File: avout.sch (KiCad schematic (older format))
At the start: 24 parts, among them CN6 AUDIO_VIDEO, M1 Modulator, Q3 2SC1815

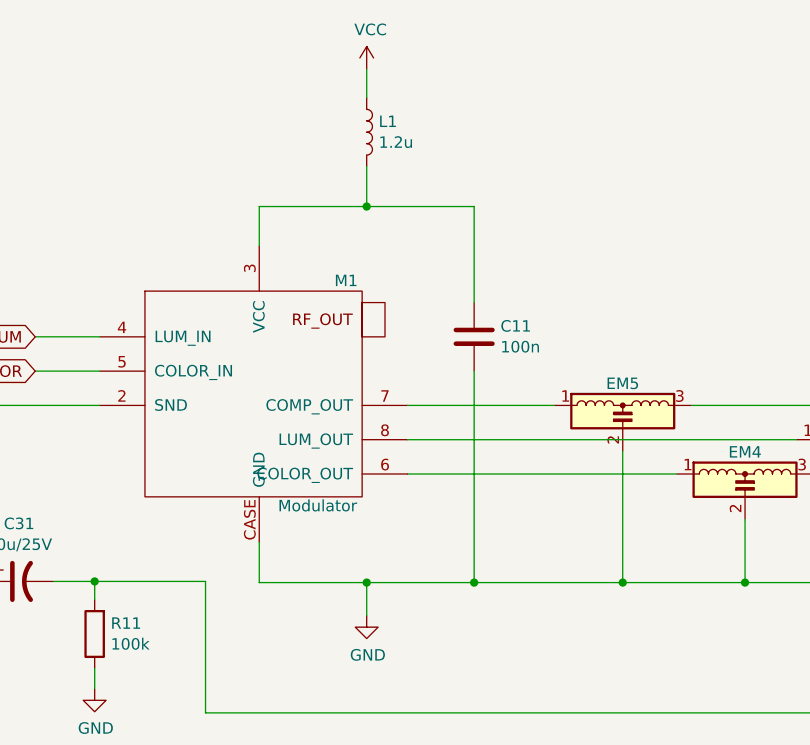
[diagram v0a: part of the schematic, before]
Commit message: Fix some errors pointed out by bwack in #1
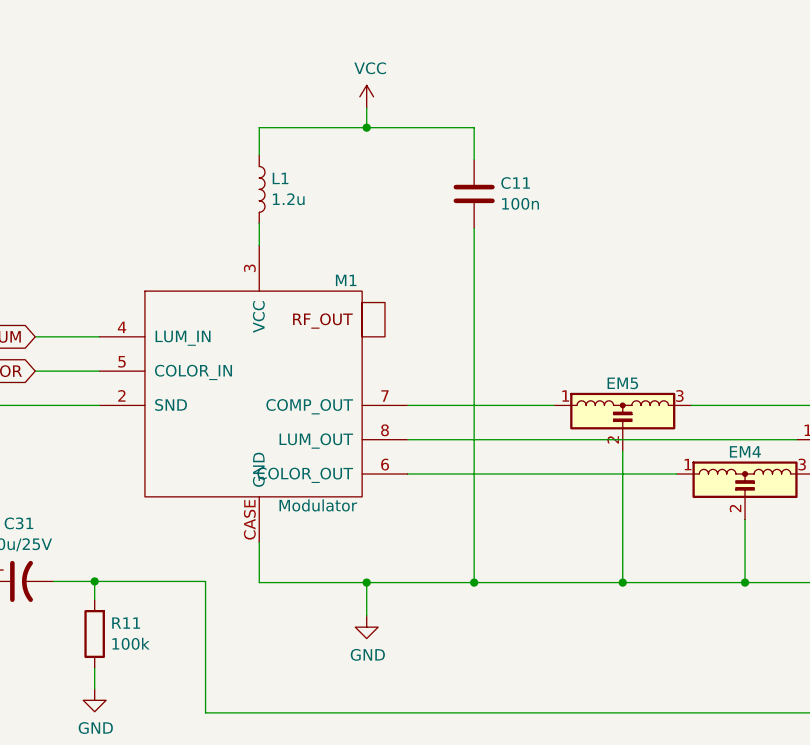
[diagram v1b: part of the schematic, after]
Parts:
- C11, C20: footprint (none) -> Capacitor_THT:C_Disc_D8.0mm_W2.5mm_P5.00mm
- C18, C19: footprint (none) -> Capacitor_THT:CP_Radial_D5.0mm_P2.50mm
- C31: footprint (none) -> Capacitor_THT:CP_Radial_D6.3mm_P2.50mm
- CN6: footprint (none) -> CommodorePlus4:Connector_DIN_Female_8Pin_3rows
- EM3, EM4, EM5: footprint (none) -> LittleSixteen:EMI_Filter
- FB12, FB13, FB58: footprint (none) -> LittleSixteen:Ferrite
- M1: footprint (none) -> CommodorePlus4:RF_Modulator
- Q3: footprint Package_TO_SOT_THT:TO-92_Inline -> Package_TO_SOT_THT:TO-92_Inline_Wide
- R11, R23, R24, R25, R26, R27, R28, R8, R9: footprint (none) -> Resistor_THT:R_Axial_DIN0207_L6.3mm_D2.5mm_P5.08mm_Vertical
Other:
- moved on the sheet: C11, L1
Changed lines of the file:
@@
 Sheet 11 11
 Title "LittleSixteen"
-Date "2020-01-03"
+Date "2020-10-04"
 Rev "1git"
 Comp "SukkoPera"
@@
 F 0 "M1" H 6440 3425 50  0000 C CNN
 F 1 "Modulator" H 6315 2440 50  0000 C CNN
-F 2 "" H 6260 2980 50  0001 C CNN
+F 2 "CommodorePlus4:RF_Modulator" H 6260 2980 50  0001 C CNN
 F 3 "" H 6260 2980 50  0001 C CNN
 	1    6060 2930
@@
 L Device:C C11
 U 1 1 5E01CA58
-P 7000 2680
-F 0 "C11" H 7115 2726 50  0000 L CNN
-F 1 "100n" H 7115 2635 50  0000 L CNN
-F 2 "" H 7038 2530 50  0001 C CNN
-F 3 "~" H 7000 2680 50  0001 C CNN
-	1    7000 2680
-	1    0    0    -1
-$EndComp
-Wire Wire Line
-	6060 2110 6530 2110
-Wire Wire Line
-	7000 2110 7000 2530
-Wire Wire Line
-	7000 2830 7000 3755
+P 7000 2055
+F 0 "C11" H 7115 2101 50  0000 L CNN
+F 1 "100n" H 7115 2010 50  0000 L CNN
+F 2 "Capacitor_THT:C_Disc_D8.0mm_W2.5mm_P5.00mm" H 7038 1905 50  0001 C CNN
+F 3 "~" H 7000 2055 50  0001 C CNN
+	1    7000 2055
+	1    0    0    -1
+$EndComp
+Wire Wire Line
+	7000 2205 7000 3755
 Wire Wire Line
 	7000 3755 6530 3755
@@
 L Device:L L1
 U 1 1 5E01E939
-P 6530 1785
-F 0 "L1" H 6582 1831 50  0000 L CNN
-F 1 "1.2u" H 6582 1740 50  0000 L CNN
-F 2 "" H 6530 1785 50  0001 C CNN
-F 3 "~" H 6530 1785 50  0001 C CNN
-	1    6530 1785
-	1    0    0    -1
-$EndComp
-Wire Wire Line
-	6530 1935 6530 2110
-Connection ~ 6530 2110
-Wire Wire Line
-	6530 2110 7000 2110
+P 6060 2035
+F 0 "L1" H 6112 2081 50  0000 L CNN
+F 1 "1.2u" H 6112 1990 50  0000 L CNN
+F 2 "" H 6060 2035 50  0001 C CNN
+F 3 "~" H 6060 2035 50  0001 C CNN
+	1    6060 2035
+	1    0    0    -1
+$EndComp
 $Comp
 L power:VCC #PWR0178
 U 1 1 5E021287
-P 6530 1510
-F 0 "#PWR0178" H 6530 1360 50  0001 C CNN
-F 1 "VCC" H 6547 1683 50  0000 C CNN
-F 2 "" H 6530 1510 50  0001 C CNN
-F 3 "" H 6530 1510 50  0001 C CNN
-	1    6530 1510
-	1    0    0    -1
-$EndComp
-Wire Wire Line
-	6530 1510 6530 1635
+P 6530 1680
+F 0 "#PWR0178" H 6530 1530 50  0001 C CNN
+F 1 "VCC" H 6547 1853 50  0000 C CNN
+F 2 "" H 6530 1680 50  0001 C CNN
+F 3 "" H 6530 1680 50  0001 C CNN
+	1    6530 1680
+	1    0    0    -1
+$EndComp
+Wire Wire Line
+	6530 1680 6530 1765
 $Comp
 L Connector:DIN-8 CN6
@@
 F 0 "CN6" H 9695 3725 50  0000 C CNN
 F 1 "AUDIO_VIDEO" H 9695 3640 50  0000 C CNN
-F 2 "" H 9695 3130 50  0001 C CNN
+F 2 "CommodorePlus4:Connector_DIN_Female_8Pin_3rows" H 9695 3130 50  0001 C CNN
 F 3 "http://www.mouser.com/ds/2/18/40_c091_abd_e-75918.pdf" H 9695 3130 50  0001 C CNN
 	1    9695 3130
@@
 F 0 "EM5" H 7650 3275 50  0000 C CNN
 F 1 "EMI_Filter_LCL" H 7650 3306 50  0001 C CNN
-F 2 "" V 7650 3080 50  0001 C CNN
+F 2 "LittleSixteen:EMI_Filter" V 7650 3080 50  0001 C CNN
 F 3 "http://www.murata.com/~/media/webrenewal/support/library/catalog/products/emc/emifil/c31e.ashx?la=en-gb" V 7650 3080 50  0001 C CNN
 	1    7650 3080
@@
 F 0 "EM3" H 8710 3425 50  0000 C CNN
 F 1 "EMI_Filter_LCL" H 8710 3456 50  0001 C CNN
-F 2 "" V 8710 3230 50  0001 C CNN
+F 2 "LittleSixteen:EMI_Filter" V 8710 3230 50  0001 C CNN
 F 3 "http://www.murata.com/~/media/webrenewal/support/library/catalog/products/emc/emifil/c31e.ashx?la=en-gb" V 8710 3230 50  0001 C CNN
 	1    8710 3230
@@
 F 0 "EM4" H 8185 3575 50  0000 C CNN
 F 1 "EMI_Filter_LCL" H 8185 3606 50  0001 C CNN
-F 2 "" V 8185 3380 50  0001 C CNN
+F 2 "LittleSixteen:EMI_Filter" V 8185 3380 50  0001 C CNN
 F 3 "http://www.murata.com/~/media/webrenewal/support/library/catalog/products/emc/emifil/c31e.ashx?la=en-gb" V 8185 3380 50  0001 C CNN
 	1    8185 3380
@@
 F 0 "FB13" H 10200 3530 50  0000 L CNN
 F 1 "Ferrite_Bead_Small" H 10200 3485 50  0001 L CNN
-F 2 "" V 10030 3530 50  0001 C CNN
+F 2 "LittleSixteen:Ferrite" V 10030 3530 50  0001 C CNN
 F 3 "~" H 10100 3530 50  0001 C CNN
 	1    10100 3530
@@
 F 0 "FB12" V 10360 3130 50  0000 C CNN
 F 1 "Ferrite_Bead_Small" H 10605 3085 50  0001 L CNN
-F 2 "" V 10435 3130 50  0001 C CNN
+F 2 "LittleSixteen:Ferrite" V 10435 3130 50  0001 C CNN
 F 3 "~" H 10505 3130 50  0001 C CNN
 	1    10505 3130
@@
 F 0 "FB58" V 10160 3030 50  0000 C CNN
 F 1 "Ferrite_Bead_Small" H 10405 2985 50  0001 L CNN
-F 2 "" V 10235 3030 50  0001 C CNN
+F 2 "LittleSixteen:Ferrite" V 10235 3030 50  0001 C CNN
 F 3 "~" H 10305 3030 50  0001 C CNN
 	1    10305 3030
@@
 F 0 "R28" V 1568 2780 50  0000 C CNN
 F 1 "1k" V 1659 2780 50  0000 C CNN
-F 2 "" V 1705 2780 50  0001 C CNN
+F 2 "Resistor_THT:R_Axial_DIN0207_L6.3mm_D2.5mm_P5.08mm_Vertical" V 1705 2780 50  0001 C CNN
 F 3 "~" H 1775 2780 50  0001 C CNN
 	1    1775 2780
@@
 F 0 "R25" H 1570 3046 50  0000 L CNN
 F 1 "100k" H 1570 2955 50  0000 L CNN
-F 2 "" V 1430 3000 50  0001 C CNN
+F 2 "Resistor_THT:R_Axial_DIN0207_L6.3mm_D2.5mm_P5.08mm_Vertical" V 1430 3000 50  0001 C CNN
 F 3 "~" H 1500 3000 50  0001 C CNN
 	1    1500 3000
@@
 F 0 "C18" V 1943 2780 50  0000 C CNN
 F 1 "10u/25V" V 2034 2780 50  0000 C CNN
-F 2 "" H 2195 2780 50  0001 C CNN
+F 2 "Capacitor_THT:CP_Radial_D5.0mm_P2.50mm" H 2195 2780 50  0001 C CNN
 F 3 "~" H 2195 2780 50  0001 C CNN
 	1    2195 2780
@@
 F 0 "R8" V 1568 2265 50  0000 C CNN
 F 1 "1k" V 1659 2265 50  0000 C CNN
-F 2 "" V 1705 2265 50  0001 C CNN
+F 2 "Resistor_THT:R_Axial_DIN0207_L6.3mm_D2.5mm_P5.08mm_Vertical" V 1705 2265 50  0001 C CNN
 F 3 "~" H 1775 2265 50  0001 C CNN
 	1    1775 2265
@@
 F 0 "C19" V 1943 2265 50  0000 C CNN
 F 1 "10u/25V" V 2034 2265 50  0000 C CNN
-F 2 "" H 2195 2265 50  0001 C CNN
+F 2 "Capacitor_THT:CP_Radial_D5.0mm_P2.50mm" H 2195 2265 50  0001 C CNN
 F 3 "~" H 2195 2265 50  0001 C CNN
 	1    2195 2265
@@
 F 0 "R24" V 3298 2515 50  0000 C CNN
 F 1 "1k" V 3389 2515 50  0000 C CNN
-F 2 "" V 3435 2515 50  0001 C CNN
+F 2 "Resistor_THT:R_Axial_DIN0207_L6.3mm_D2.5mm_P5.08mm_Vertical" V 3435 2515 50  0001 C CNN
 F 3 "~" H 3505 2515 50  0001 C CNN
 	1    3505 2515
@@
 F 0 "R9" H 2905 2826 50  0000 L CNN
 F 1 "12k" H 2905 2735 50  0000 L CNN
-F 2 "" V 2765 2780 50  0001 C CNN
+F 2 "Resistor_THT:R_Axial_DIN0207_L6.3mm_D2.5mm_P5.08mm_Vertical" V 2765 2780 50  0001 C CNN
 F 3 "~" H 2835 2780 50  0001 C CNN
 	1    2835 2780
@@
 F 0 "C20" H 3255 2826 50  0000 L CNN
 F 1 "10n" H 3255 2735 50  0000 L CNN
-F 2 "" H 3178 2630 50  0001 C CNN
+F 2 "Capacitor_THT:C_Disc_D8.0mm_W2.5mm_P5.00mm" H 3178 2630 50  0001 C CNN
 F 3 "~" H 3140 2780 50  0001 C CNN
 	1    3140 2780
@@
 F 0 "Q3" H 4180 2561 50  0000 L CNN
 F 1 "2SC1815" H 4180 2470 50  0000 L CNN
-F 2 "Package_TO_SOT_THT:TO-92_Inline" H 4190 2440 50  0001 L CIN
+F 2 "Package_TO_SOT_THT:TO-92_Inline_Wide" H 4190 2440 50  0001 L CIN
 F 3 "https://media.digikey.com/pdf/Data%20Sheets/Toshiba%20PDFs/2SC1815.pdf" H 3990 2515 50  0001 L CNN
 	1    3990 2515
@@
 F 0 "R23" H 3210 2246 50  0000 L CNN
 F 1 "10k" H 3210 2155 50  0000 L CNN
-F 2 "" V 3070 2200 50  0001 C CNN
+F 2 "Resistor_THT:R_Axial_DIN0207_L6.3mm_D2.5mm_P5.08mm_Vertical" V 3070 2200 50  0001 C CNN
 F 3 "~" H 3140 2200 50  0001 C CNN
 	1    3140 2200
@@
 F 0 "R26" V 4133 3750 50  0000 C CNN
 F 1 "240" V 4224 3750 50  0000 C CNN
-F 2 "" V 4270 3750 50  0001 C CNN
+F 2 "Resistor_THT:R_Axial_DIN0207_L6.3mm_D2.5mm_P5.08mm_Vertical" V 4270 3750 50  0001 C CNN
 F 3 "~" H 4340 3750 50  0001 C CNN
 	1    4340 3750
@@
 F 0 "R27" H 4600 3934 50  0000 R CNN
 F 1 "240" H 4600 4025 50  0000 R CNN
-F 2 "" V 4600 3980 50  0001 C CNN
+F 2 "Resistor_THT:R_Axial_DIN0207_L6.3mm_D2.5mm_P5.08mm_Vertical" V 4600 3980 50  0001 C CNN
 F 3 "~" H 4670 3980 50  0001 C CNN
 	1    4670 3980
@@
 F 0 "C31" V 4758 3750 50  0000 C CNN
 F 1 "10u/25V" V 4849 3750 50  0000 C CNN
-F 2 "" H 5010 3750 50  0001 C CNN
+F 2 "Capacitor_THT:CP_Radial_D6.3mm_P2.50mm" H 5010 3750 50  0001 C CNN
 F 3 "~" H 5010 3750 50  0001 C CNN
 	1    5010 3750
@@
 F 0 "R11" H 5270 3934 50  0000 R CNN
 F 1 "100k" H 5270 4025 50  0000 R CNN
-F 2 "" V 5270 3980 50  0001 C CNN
+F 2 "Resistor_THT:R_Axial_DIN0207_L6.3mm_D2.5mm_P5.08mm_Vertical" V 5270 3980 50  0001 C CNN
 F 3 "~" H 5340 3980 50  0001 C CNN
 	1    5340 3980
@@
 	4090 1780 4090 1875
 Connection ~ 4090 1875
-Wire Wire Line
-	6060 2280 6060 2110
 Text Notes 10670 3010 0    50   ~ 0
 EXT_AUDIO
@@
 Text Notes 8575 2360 0    50   ~ 0
 From C64-Wiki (C64 uses the same connector):\n\nThe eight pin jack is *not* the more common DIN 45326\n(pins spanning 270°, circular like a horseshoe), but\nDIN 41524 (pins spanning 262°, a "U" shape with a more\nopen end). It's possible to forcibly plug in a wrong plug into\nthe jack, but one should get the right plug in the first place\non a new purchase. Should you happen to get the wrong\nplug and wasn't planning to use the +5V pin then you can\nremove the upper two pins out for a perfect fit.
+Wire Wire Line
+	6530 1765 7000 1765
+Connection ~ 6530 1765
+Wire Wire Line
+	7000 1765 7000 1905
+Wire Wire Line
+	6530 1765 6060 1765
+Wire Wire Line
+	6060 1765 6060 1885
+Wire Wire Line
+	6060 2185 6060 2280
 $EndSCHEMATC

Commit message: Start working on PCB
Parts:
- C18, C19: footprint Capacitor_THT:CP_Radial_D5.0mm_P2.50mm -> Capacitor_THT:CP_Radial_D6.3mm_P2.50mm
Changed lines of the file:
@@
 F 0 "C18" V 1943 2780 50  0000 C CNN
 F 1 "10u/25V" V 2034 2780 50  0000 C CNN
-F 2 "Capacitor_THT:CP_Radial_D5.0mm_P2.50mm" H 2195 2780 50  0001 C CNN
+F 2 "Capacitor_THT:CP_Radial_D6.3mm_P2.50mm" H 2195 2780 50  0001 C CNN
 F 3 "~" H 2195 2780 50  0001 C CNN
 	1    2195 2780
@@
 F 0 "C19" V 1943 2265 50  0000 C CNN
 F 1 "10u/25V" V 2034 2265 50  0000 C CNN
-F 2 "Capacitor_THT:CP_Radial_D5.0mm_P2.50mm" H 2195 2265 50  0001 C CNN
+F 2 "Capacitor_THT:CP_Radial_D6.3mm_P2.50mm" H 2195 2265 50  0001 C CNN
 F 3 "~" H 2195 2265 50  0001 C CNN
 	1    2195 2265

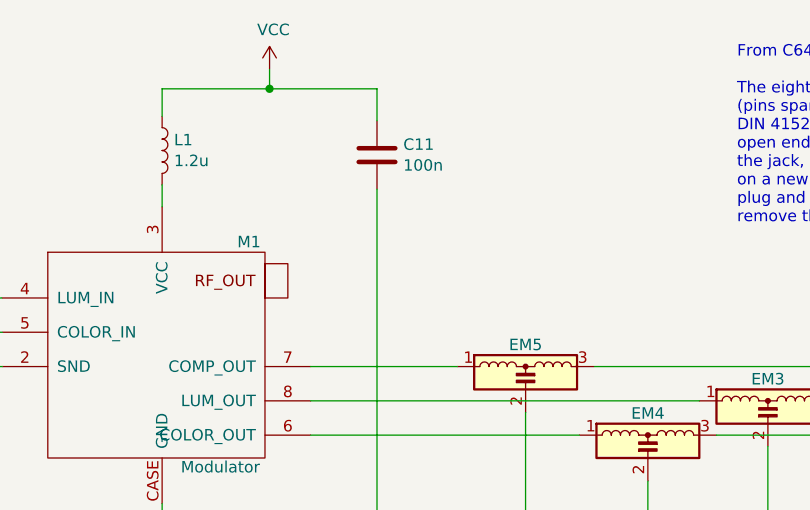
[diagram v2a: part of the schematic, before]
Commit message: Add ceramics
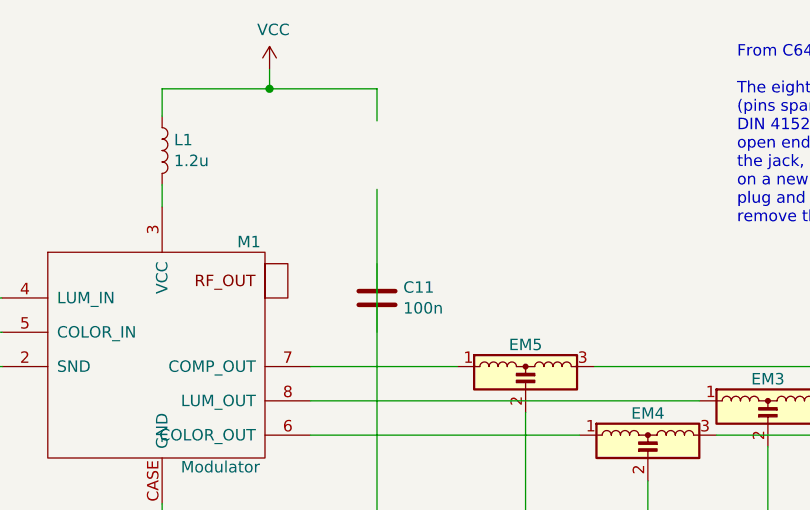
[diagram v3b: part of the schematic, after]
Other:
- moved on the sheet: C11
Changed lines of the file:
@@
 L Device:C C11
 U 1 1 5E01CA58
-P 7000 2055
-F 0 "C11" H 7115 2101 50  0000 L CNN
-F 1 "100n" H 7115 2010 50  0000 L CNN
-F 2 "Capacitor_THT:C_Disc_D8.0mm_W2.5mm_P5.00mm" H 7038 1905 50  0001 C CNN
-F 3 "~" H 7000 2055 50  0001 C CNN
-	1    7000 2055
+P 7000 2680
+F 0 "C11" H 7115 2726 50  0000 L CNN
+F 1 "100n" H 7115 2635 50  0000 L CNN
+F 2 "Capacitor_THT:C_Disc_D8.0mm_W2.5mm_P5.00mm" H 7038 2530 50  0001 C CNN
+F 3 "~" H 7000 2680 50  0001 C CNN
+	1    7000 2680
 	1    0    0    -1
 $EndComp

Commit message: Add crystal
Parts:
- C18, C19: footprint Capacitor_THT:CP_Radial_D6.3mm_P2.50mm -> Capacitor_THT:CP_Radial_D5.0mm_P2.50mm
- EM3, EM4, EM5: footprint LittleSixteen:EMI_Filter -> CSeventeen:EMI_Filter
- FB12, FB13, FB58: footprint LittleSixteen:Ferrite -> CSeventeen:Ferrite
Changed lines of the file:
@@
 F 0 "EM5" H 7650 3275 50  0000 C CNN
 F 1 "EMI_Filter_LCL" H 7650 3306 50  0001 C CNN
-F 2 "LittleSixteen:EMI_Filter" V 7650 3080 50  0001 C CNN
+F 2 "CSeventeen:EMI_Filter" V 7650 3080 50  0001 C CNN
 F 3 "http://www.murata.com/~/media/webrenewal/support/library/catalog/products/emc/emifil/c31e.ashx?la=en-gb" V 7650 3080 50  0001 C CNN
 	1    7650 3080
@@
 F 0 "EM3" H 8710 3425 50  0000 C CNN
 F 1 "EMI_Filter_LCL" H 8710 3456 50  0001 C CNN
-F 2 "LittleSixteen:EMI_Filter" V 8710 3230 50  0001 C CNN
+F 2 "CSeventeen:EMI_Filter" V 8710 3230 50  0001 C CNN
 F 3 "http://www.murata.com/~/media/webrenewal/support/library/catalog/products/emc/emifil/c31e.ashx?la=en-gb" V 8710 3230 50  0001 C CNN
 	1    8710 3230
@@
 F 0 "EM4" H 8185 3575 50  0000 C CNN
 F 1 "EMI_Filter_LCL" H 8185 3606 50  0001 C CNN
-F 2 "LittleSixteen:EMI_Filter" V 8185 3380 50  0001 C CNN
+F 2 "CSeventeen:EMI_Filter" V 8185 3380 50  0001 C CNN
 F 3 "http://www.murata.com/~/media/webrenewal/support/library/catalog/products/emc/emifil/c31e.ashx?la=en-gb" V 8185 3380 50  0001 C CNN
 	1    8185 3380
@@
 F 0 "FB13" H 10200 3530 50  0000 L CNN
 F 1 "Ferrite_Bead_Small" H 10200 3485 50  0001 L CNN
-F 2 "LittleSixteen:Ferrite" V 10030 3530 50  0001 C CNN
+F 2 "CSeventeen:Ferrite" V 10030 3530 50  0001 C CNN
 F 3 "~" H 10100 3530 50  0001 C CNN
 	1    10100 3530
@@
 F 0 "FB12" V 10360 3130 50  0000 C CNN
 F 1 "Ferrite_Bead_Small" H 10605 3085 50  0001 L CNN
-F 2 "LittleSixteen:Ferrite" V 10435 3130 50  0001 C CNN
+F 2 "CSeventeen:Ferrite" V 10435 3130 50  0001 C CNN
 F 3 "~" H 10505 3130 50  0001 C CNN
 	1    10505 3130
@@
 F 0 "FB58" V 10160 3030 50  0000 C CNN
 F 1 "Ferrite_Bead_Small" H 10405 2985 50  0001 L CNN
-F 2 "LittleSixteen:Ferrite" V 10235 3030 50  0001 C CNN
+F 2 "CSeventeen:Ferrite" V 10235 3030 50  0001 C CNN
 F 3 "~" H 10305 3030 50  0001 C CNN
 	1    10305 3030
@@
 F 0 "C18" V 1943 2780 50  0000 C CNN
 F 1 "10u/25V" V 2034 2780 50  0000 C CNN
-F 2 "Capacitor_THT:CP_Radial_D6.3mm_P2.50mm" H 2195 2780 50  0001 C CNN
+F 2 "Capacitor_THT:CP_Radial_D5.0mm_P2.50mm" H 2195 2780 50  0001 C CNN
 F 3 "~" H 2195 2780 50  0001 C CNN
 	1    2195 2780
@@
 F 0 "C19" V 1943 2265 50  0000 C CNN
 F 1 "10u/25V" V 2034 2265 50  0000 C CNN
-F 2 "Capacitor_THT:CP_Radial_D6.3mm_P2.50mm" H 2195 2265 50  0001 C CNN
+F 2 "Capacitor_THT:CP_Radial_D5.0mm_P2.50mm" H 2195 2265 50  0001 C CNN
 F 3 "~" H 2195 2265 50  0001 C CNN
 	1    2195 2265

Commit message: CSeventeen -> LittleSixteen (PCB)
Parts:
- EM3, EM4, EM5: footprint CSeventeen:EMI_Filter -> LittleSixteen:EMI_Filter
- FB12, FB13, FB58: footprint CSeventeen:Ferrite -> LittleSixteen:Ferrite
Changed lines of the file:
@@
 F 0 "EM5" H 7650 3275 50  0000 C CNN
 F 1 "EMI_Filter_LCL" H 7650 3306 50  0001 C CNN
-F 2 "CSeventeen:EMI_Filter" V 7650 3080 50  0001 C CNN
+F 2 "LittleSixteen:EMI_Filter" V 7650 3080 50  0001 C CNN
 F 3 "http://www.murata.com/~/media/webrenewal/support/library/catalog/products/emc/emifil/c31e.ashx?la=en-gb" V 7650 3080 50  0001 C CNN
 	1    7650 3080
@@
 F 0 "EM3" H 8710 3425 50  0000 C CNN
 F 1 "EMI_Filter_LCL" H 8710 3456 50  0001 C CNN
-F 2 "CSeventeen:EMI_Filter" V 8710 3230 50  0001 C CNN
+F 2 "LittleSixteen:EMI_Filter" V 8710 3230 50  0001 C CNN
 F 3 "http://www.murata.com/~/media/webrenewal/support/library/catalog/products/emc/emifil/c31e.ashx?la=en-gb" V 8710 3230 50  0001 C CNN
 	1    8710 3230
@@
 F 0 "EM4" H 8185 3575 50  0000 C CNN
 F 1 "EMI_Filter_LCL" H 8185 3606 50  0001 C CNN
-F 2 "CSeventeen:EMI_Filter" V 8185 3380 50  0001 C CNN
+F 2 "LittleSixteen:EMI_Filter" V 8185 3380 50  0001 C CNN
 F 3 "http://www.murata.com/~/media/webrenewal/support/library/catalog/products/emc/emifil/c31e.ashx?la=en-gb" V 8185 3380 50  0001 C CNN
 	1    8185 3380
@@
 F 0 "FB13" H 10200 3530 50  0000 L CNN
 F 1 "Ferrite_Bead_Small" H 10200 3485 50  0001 L CNN
-F 2 "CSeventeen:Ferrite" V 10030 3530 50  0001 C CNN
+F 2 "LittleSixteen:Ferrite" V 10030 3530 50  0001 C CNN
 F 3 "~" H 10100 3530 50  0001 C CNN
 	1    10100 3530
@@
 F 0 "FB12" V 10360 3130 50  0000 C CNN
 F 1 "Ferrite_Bead_Small" H 10605 3085 50  0001 L CNN
-F 2 "CSeventeen:Ferrite" V 10435 3130 50  0001 C CNN
+F 2 "LittleSixteen:Ferrite" V 10435 3130 50  0001 C CNN
 F 3 "~" H 10505 3130 50  0001 C CNN
 	1    10505 3130
@@
 F 0 "FB58" V 10160 3030 50  0000 C CNN
 F 1 "Ferrite_Bead_Small" H 10405 2985 50  0001 L CNN
-F 2 "CSeventeen:Ferrite" V 10235 3030 50  0001 C CNN
+F 2 "LittleSixteen:Ferrite" V 10235 3030 50  0001 C CNN
 F 3 "~" H 10305 3030 50  0001 C CNN
 	1    10305 3030

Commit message: Working on PCB...
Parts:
- L1: footprint (none) -> Inductor_THT:L_Axial_L7.0mm_D3.3mm_P12.70mm_Horizontal_Fastron_MICC
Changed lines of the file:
@@
 F 0 "L1" H 6112 2081 50  0000 L CNN
 F 1 "1.2u" H 6112 1990 50  0000 L CNN
-F 2 "" H 6060 2035 50  0001 C CNN
+F 2 "Inductor_THT:L_Axial_L7.0mm_D3.3mm_P12.70mm_Horizontal_Fastron_MICC" H 6060 2035 50  0001 C CNN
 F 3 "~" H 6060 2035 50  0001 C CNN
 	1    6060 2035
@@
 F 3 "http://www.murata.com/~/media/webrenewal/support/library/catalog/products/emc/emifil/c31e.ashx?la=en-gb" V 7650 3080 50  0001 C CNN
 	1    7650 3080
-	1    0    0    -1
+	-1   0    0    -1
 $EndComp
 $Comp
@@
 F 3 "http://www.murata.com/~/media/webrenewal/support/library/catalog/products/emc/emifil/c31e.ashx?la=en-gb" V 8710 3230 50  0001 C CNN
 	1    8710 3230
-	1    0    0    -1
+	-1   0    0    -1
 $EndComp
 $Comp
@@
 F 3 "http://www.murata.com/~/media/webrenewal/support/library/catalog/products/emc/emifil/c31e.ashx?la=en-gb" V 8185 3380 50  0001 C CNN
 	1    8185 3380
-	1    0    0    -1
+	-1   0    0    -1
 $EndComp
 Wire Wire Line
@@
 F 3 "~" H 10505 3130 50  0001 C CNN
 	1    10505 3130
-	0    1    1    0
+	0    -1   1    0
 $EndComp
 $Comp
@@
 F 3 "~" H 10305 3030 50  0001 C CNN
 	1    10305 3030
-	0    1    1    0
+	0    -1   1    0
 $EndComp
 Wire Wire Line
@@
 U 1 1 5E067484
 P 3505 2515
-F 0 "R24" V 3298 2515 50  0000 C CNN
-F 1 "1k" V 3389 2515 50  0000 C CNN
+F 0 "R24" V 3712 2515 50  0000 C CNN
+F 1 "1k" V 3621 2515 50  0000 C CNN
 F 2 "Resistor_THT:R_Axial_DIN0207_L6.3mm_D2.5mm_P5.08mm_Vertical" V 3435 2515 50  0001 C CNN
 F 3 "~" H 3505 2515 50  0001 C CNN
 	1    3505 2515
-	0    1    1    0
-$EndComp
-$Comp
+	0    -1   -1   0
+$EndComp
+$Comp
